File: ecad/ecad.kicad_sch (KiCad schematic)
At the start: 45 parts, among them J1 USB_C, J2 UART, J3 POWER, Q1 DMN3009SFG, Q2 DMN3009SFG, SW1 RESET, SW2 BOOT, U1 TPD4E02B04DQA, U2 AP33772S, U3 AP63203WU, U4 PCA9306, U5 ESP32-C3

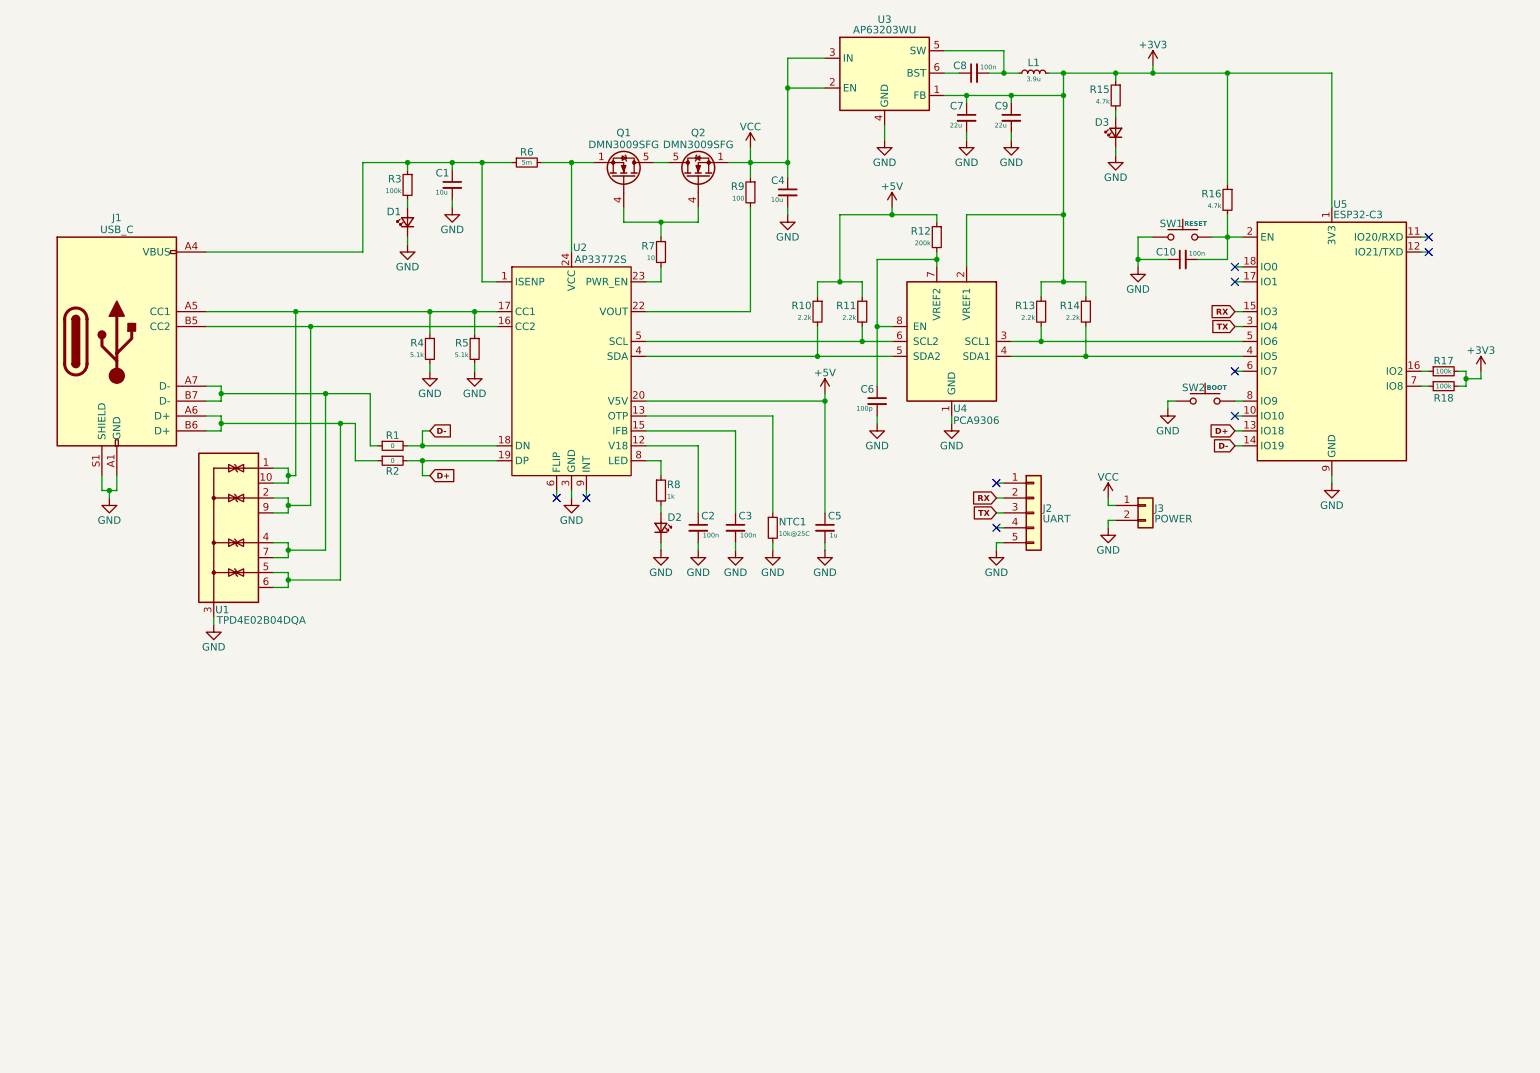
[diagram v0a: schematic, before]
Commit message: ecad: gerber folder, espressif lib and some pcb design
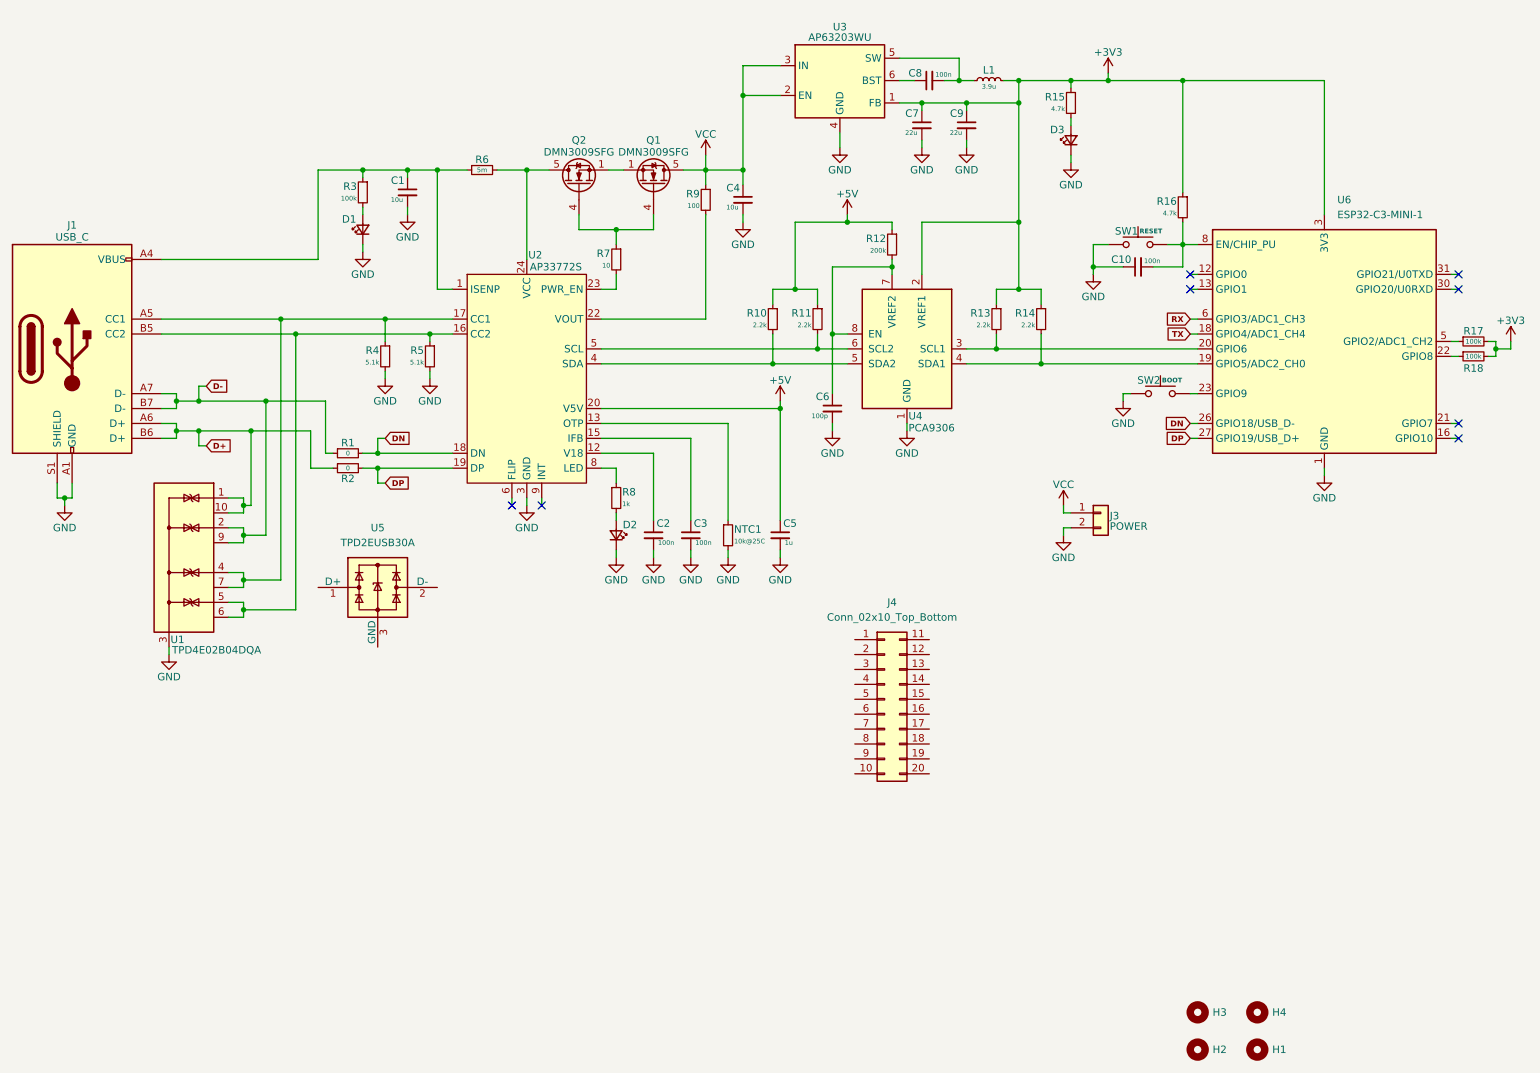
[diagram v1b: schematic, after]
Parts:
- removed J2: UART, Connector_JST:JST_PH_B4B-PH-K_1x04_P2.00mm_Vertical, symbol Connector_Generic:Conn_01x05
- removed U5: ESP32-C3, RF_Module:ESP32-C3-WROOM-02, symbol RF_Module:ESP32-C3-WROOM-02
- added H1, H2, H3, H4: MountingHole, MountingHole:MountingHole_2.2mm_M2_Pad_TopBottom, symbol Mechanical:MountingHole
- added J4: Conn_02x10_Top_Bottom, Connector_PinSocket_2.54mm:PinSocket_2x10_P2.54mm_Vertical, symbol Connector_Generic:Conn_02x10_Top_Bottom
- added U5: TPD2EUSB30A, Package_TO_SOT_SMD:Texas_DRT-3, symbol Power_Protection:TPD2EUSB30A
- added U6: ESP32-C3-MINI-1, ESPRESSIF:ESP32-C3-MINI-1, symbol espressif:ESP32-C3-MINI-1
- C7, C9: footprint Capacitor_SMD:C_0402_1005Metric -> Capacitor_SMD:C_0805_2012Metric
- J3: footprint (none) -> TerminalBlock:TerminalBlock_bornier-2_P5.08mm
- L1: footprint Inductor_SMD:L_APV_ANR6045 -> Inductor_SMD:L_Wuerth_MAPI-3015
- R6: footprint Resistor_SMD:R_0402_1005Metric -> Resistor_SMD:R_1206_3216Metric
- U2: footprint (none) -> Package_DFN_QFN:WQFN-24-1EP_4x4mm_P0.5mm_EP2.6x2.6mm
- U4: footprint (none) -> Package_SO:VSSOP-8_2.3x2mm_P0.5mm
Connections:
- net +3V3: now also U6.3 (3V3)
- net D+: now also J1.A6 (D+), J1.B6 (D+), R2.1, U1.1 (IO1), U1.10 (NC); no longer R2.2, U2.19 (DP)
- net D-: now also J1.A7 (D-), J1.B7 (D-), R1.1, U1.2 (IO2), U1.9 (NC); no longer R1.2, U2.18 (DN)
- net GND: now also U6.1 (GND), U6.11 (GND), U6.14 (GND), U6.2 (GND), U6.36 (GND), U6.37 (GND), U6.38 (GND), U6.39 (GND), U6.40 (GND), U6.41 (GND), U6.42 (GND), U6.43 (GND), U6.44 (GND), U6.45 (GND), U6.46 (GND), U6.47 (GND), U6.48 (GND), U6.49 (GND), U6.50 (GND), U6.51 (GND), U6.52 (GND), U6.53 (GND)
- net RX: now also U6.6 (GPIO3/ADC1_CH3)
- net TX: now also U6.18 (GPIO4/ADC1_CH4)
- net VCC: now also Q1.5 (D); no longer Q2.1 (S), Q2.2 (S), Q2.3 (S)
- net at Q2.5 (D): now also R6.2, U2.24 (VCC); no longer Q1.5 (D)
- net at R13.2, U4.3 (SCL1): now also U6.20 (GPIO6)
- net at R14.2, U4.4 (SDA1): now also U6.19 (GPIO5/ADC2_CH0)
- net at Q1.1 (S), Q1.2 (S), Q1.3 (S): now also Q2.1 (S), Q2.2 (S), Q2.3 (S); no longer R6.2, U2.24 (VCC)
- net at C10.2, R16.2, SW1.2: now also U6.8 (EN/CHIP_PU)
- net at J1.A5 (CC1), R4.1, U2.17 (CC1): now also U1.4 (IO3), U1.7 (NC); no longer R5.1, U1.1 (IO1), U1.10 (NC)
- net at J1.B5 (CC2), U2.16 (CC2): now also R5.1, U1.5 (IO4), U1.6 (NC); no longer U1.2 (IO2), U1.9 (NC)
- net at SW2.2: now also U6.23 (GPIO9)
- net at R17.1: now also U6.5 (GPIO2/ADC1_CH2)
- net at R18.1: now also U6.22 (GPIO8)
- new net DN: R1.2, U2.18 (DN), U6.26 (GPIO18/USB_D-)
- new net DP: R2.2, U2.19 (DP), U6.27 (GPIO19/USB_D+)
- no-connect marks 10 -> 8
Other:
- moved on the sheet: C1, C10, C2, C3, C4, C5, C6, C7, C8, C9, D1, D2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

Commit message: ecad: 4 layers setup and more routing
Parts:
- removed U5: TPD2EUSB30A, Package_TO_SOT_SMD:Texas_DRT-3, symbol Power_Protection:TPD2EUSB30A
- U2: footprint Package_DFN_QFN:WQFN-24-1EP_4x4mm_P0.5mm_EP2.6x2.6mm -> Package_DFN_QFN:WQFN-24-1EP_4x4mm_P0.5mm_EP2.6x2.6mm_ThermalVias
- U4: footprint Package_SO:VSSOP-8_2.3x2mm_P0.5mm -> Package_SO:TSSOP-8_3x3mm_P0.65mm
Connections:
- net I2C+: now reaches R13.2, U4.3 (SCL1), U6.20 (GPIO6)
- net I2C-: now reaches R14.2, U4.4 (SDA1), U6.19 (GPIO5/ADC2_CH0)
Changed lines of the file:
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@@
 		)
 	)
+	(label "I2C+"
+		(at 205.74 73.66 0)
+		(fields_autoplaced yes)
+		(effects
+			(font
+				(size 1.27 1.27)
+			)
+			(justify left bottom)
+		)
+	)
+	(label "I2C-"
+		(at 205.74 76.2 0)
+		(fields_autoplaced yes)
+		(effects
+			(font
+				(size 1.27 1.27)
+			)
+			(justify left bottom)
+		)
+	)
 	(global_label "D+"
 		(shape input)
@@
 			)
 		)
-		(property "Footprint" "Package_SO:VSSOP-8_2.3x2mm_P0.5mm"
+		(property "Footprint" "Package_SO:TSSOP-8_3x3mm_P0.65mm"
 			(at 185.42 64.77 0)
 			(effects
@@
 	)
 	(symbol
-		(lib_id "Power_Protection:TPD2EUSB30A")
-		(at 85.09 114.3 0)
-		(unit 1)
-		(exclude_from_sim no)
-		(in_bom yes)
-		(on_board yes)
-		(dnp no)
-		(fields_autoplaced yes)
-		(property "Reference" "U5"
-			(at 85.09 104.14 0)
-			(effects
-				(font
-					(size 1.27 1.27)
-				)
-			)
-		)
-		(property "Value" "TPD2EUSB30A"
-			(at 85.09 106.68 0)
-			(effects
-				(font
-					(size 1.27 1.27)
-				)
-			)
-		)
-		(property "Footprint" "Package_TO_SOT_SMD:Texas_DRT-3"
-			(at 66.04 121.92 0)
-			(effects
-				(font
-					(size 1.27 1.27)
-				)
-				(hide yes)
-			)
-		)
-		(property "Datasheet" "http://www.ti.com/lit/ds/symlink/tpd2eusb30a.pdf"
-			(at 85.09 114.3 0)
-			(effects
-				(font
-					(size 1.27 1.27)
-				)
-				(hide yes)
-			)
-		)
-		(property "Description" "2-Channel ESD Protection for Super-Speed USB 3.0 Interface, DRT-3"
-			(at 85.09 114.3 0)
-			(effects
-				(font
-					(size 1.27 1.27)
-				)
-				(hide yes)
-			)
-		)
-		(pin "3"
-		)
-		(pin "2"
-		)
-		(pin "1"
-		)
-		(instances
-			(project ""
-				(path "/0c3ebb9a-f0ed-4697-b9fa-e4684bc428d7"
-					(reference "U5")
-					(unit 1)
-				)
-			)
-		)
-	)
-	(symbol
 		(lib_id "Device:R_Small")
 		(at 125.73 58.42 0)
@@
 			)
 		)
-		(property "Footprint" "Package_DFN_QFN:WQFN-24-1EP_4x4mm_P0.5mm_EP2.6x2.6mm"
+		(property "Footprint" "Package_DFN_QFN:WQFN-24-1EP_4x4mm_P0.5mm_EP2.6x2.6mm_ThermalVias"
 			(at 110.49 78.74 0)
 			(effects

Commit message: ecad fix: board placement and page template
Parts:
- removed J4: Conn_02x10_Top_Bottom, Connector_PinSocket_2.54mm:PinSocket_2x10_P2.54mm_Vertical, symbol Connector_Generic:Conn_02x10_Top_Bottom
- added J2: Printer, Connector_JST:JST_PH_B5B-PH-K_1x05_P2.00mm_Vertical, symbol Connector_Generic:Conn_01x05
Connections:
- net GND: now also J2.1 (Pin_1)
- net RX: now also U6.16 (GPIO10), J2.4 (Pin_4); no longer U6.6 (GPIO3/ADC1_CH3)
- net TX: now also J2.3 (Pin_3)
- no-connect marks 8 -> 10
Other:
- title: ESP 32 Thermal Printer -> PaperFlow

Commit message: ecad fix: fix bad connection to usb
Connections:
- net D+: now also U6.27 (GPIO19/USB_D+)
- net D-: now also U6.26 (GPIO18/USB_D-)
- net DN: no longer U6.26 (GPIO18/USB_D-)
- net DP: no longer U6.27 (GPIO19/USB_D+)
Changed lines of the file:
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@@
+		)
+	)
+	(global_label "D+"
+		(shape input)
+		(at 223.52 88.9 180)
+		(fields_autoplaced yes)
+		(effects
+			(font
+				(size 1 1)
+				(thickness 0.254)
+				(bold yes)
+			)
+			(justify right)
+		)
+		(property "Intersheetrefs" "${INTERSHEET_REFS}"
+			(at 218.3066 88.9 0)
+			(effects
+				(font
+					(size 1.27 1.27)
+				)
+				(justify right)
+				(hide yes)
+			)
 		)
 	)
@@
 				)
 				(justify left)
-				(hide yes)
-			)
-		)
-	)
-	(global_label "DP"
-		(shape input)
-		(at 223.52 88.9 180)
-		(fields_autoplaced yes)
-		(effects
-			(font
-				(size 1 1)
-				(thickness 0.254)
-				(bold yes)
-			)
-			(justify right)
-		)
-		(property "Intersheetrefs" "${INTERSHEET_REFS}"
-			(at 218.5447 88.9 0)
-			(effects
-				(font
-					(size 1.27 1.27)
-				)
-				(justify right)
-				(hide yes)
-			)
-		)
-	)
-	(global_label "DN"
-		(shape input)
-		(at 223.52 86.36 180)
-		(fields_autoplaced yes)
-		(effects
-			(font
-				(size 1 1)
-				(thickness 0.254)
-				(bold yes)
-			)
-			(justify right)
-		)
-		(property "Intersheetrefs" "${INTERSHEET_REFS}"
-			(at 218.4971 86.36 0)
-			(effects
-				(font
-					(size 1.27 1.27)
-				)
-				(justify right)
 				(hide yes)
 			)
@@
 			(effects
 				(font
+					(size 1.27 1.27)
+				)
+				(justify right)
+				(hide yes)
+			)
+		)
+	)
+	(global_label "D-"
+		(shape input)
+		(at 223.52 86.36 180)
+		(fields_autoplaced yes)
+		(effects
+			(font
+				(size 1 1)
+				(thickness 0.254)
+				(bold yes)
+			)
+			(justify right)
+		)
+		(property "Intersheetrefs" "${INTERSHEET_REFS}"
+			(at 218.3066 86.36 0)
+			(effects
+				(font

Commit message: ecad fix: change some reset res value according to datasheet
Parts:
- C10: value 100n -> 1u
- R16: value 4.7k -> 10k
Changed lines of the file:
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@@
 			)
 		)
-		(property "Value" "100n"
+		(property "Value" "1u"
 			(at 215.646 58.674 90)
 			(effects
@@
 			)
 		)
-		(property "Value" "4.7k"
+		(property "Value" "10k"
 			(at 221.234 50.546 0)
 			(effects
